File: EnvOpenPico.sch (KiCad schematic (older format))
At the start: 37 parts, among them J2 Conn_01x02, J3 Conn_02x18_Odd_Even, J4 Conn_02x18_Odd_Even, J5 Conn_01x03_Male, U1 SPX3819M5-L-3-3, U2 W25Q128JVPIQ, U3 RP2040, X1 XO 32 12Mhz

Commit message: Corrected some notes
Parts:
- D3: value LED 0402 -> LED 0402 YELLOW
- J2: value Conn_01x02 -> B3U-1000P
- R3, R4: value 27 -> 27 0402 Resistor
- e1: value USB_C -> TYPE-C-31-M-12
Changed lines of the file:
@@
 P 1000 1750
 F 0 "e1" H 750 2150 50  0000 R CNN
-F 1 "USB_C" H 950 950 50  0000 R CNN
+F 1 "TYPE-C-31-M-12" H 1250 950 50  0000 R CNN
 F 2 "Connector_USB:USB_C_Receptacle_HRO_TYPE-C-31-M-12" H 1150 1700 50  0001 C CNN
 F 3 "~" H 1150 1700 50  0001 C CNN
@@
 P 9650 4100
 F 0 "R4" V 9443 4100 50  0000 C CNN
-F 1 "27" V 9534 4100 50  0000 C CNN
+F 1 "27 0402 Resistor" V 9534 4100 50  0000 C CNN
 F 2 "Capacitor_SMD:C_0402_1005Metric" V 9580 4100 50  0001 C CNN
 F 3 "~" H 9650 4100 50  0001 C CNN
@@
 P 1050 4950
 F 0 "J2" H 1100 5100 50  0000 C CNN
-F 1 "Conn_01x02" H 1050 4850 50  0000 C CNN
+F 1 "B3U-1000P" H 1050 4850 50  0000 C CNN
 F 2 "Button_Switch_SMD:SW_SPST_B3U-1000P" H 1050 4950 50  0001 C CNN
 F 3 "~" H 1050 4950 50  0001 C CNN
@@
 P 9650 3800
 F 0 "R3" V 9443 3800 50  0000 C CNN
-F 1 "27" V 9534 3800 50  0000 C CNN
+F 1 "27 0402 Resistor" V 9534 3800 50  0000 C CNN
 F 2 "Capacitor_SMD:C_0402_1005Metric" V 9580 3800 50  0001 C CNN
 F 3 "~" H 9650 3800 50  0001 C CNN
@@
 P 14800 7600
 F 0 "D3" H 14750 7350 50  0000 C CNN
-F 1 "LED 0402" H 14600 7450 50  0000 C CNN
+F 1 "LED 0402 YELLOW" H 14600 7450 50  0000 C CNN
 F 2 "LED_SMD:LED_0402_1005Metric" H 14800 7600 50  0001 C CNN
 F 3 "~" H 14800 7600 50  0001 C CNN

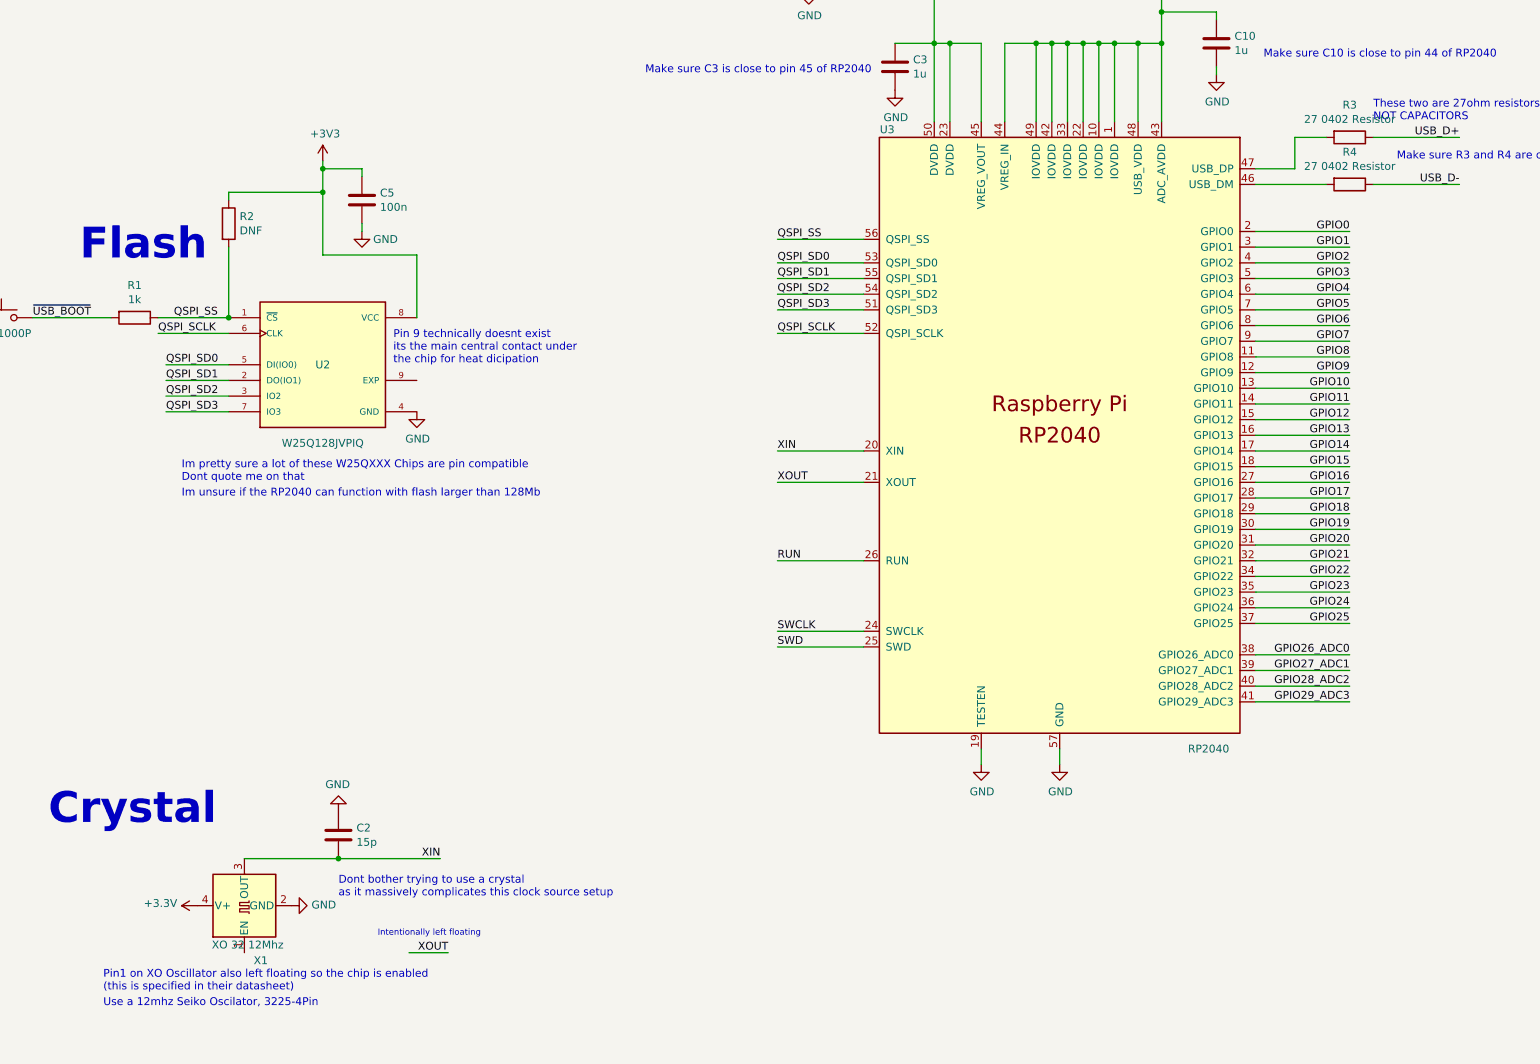
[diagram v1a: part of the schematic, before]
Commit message: Adjusted lables and notes some more for BOM export
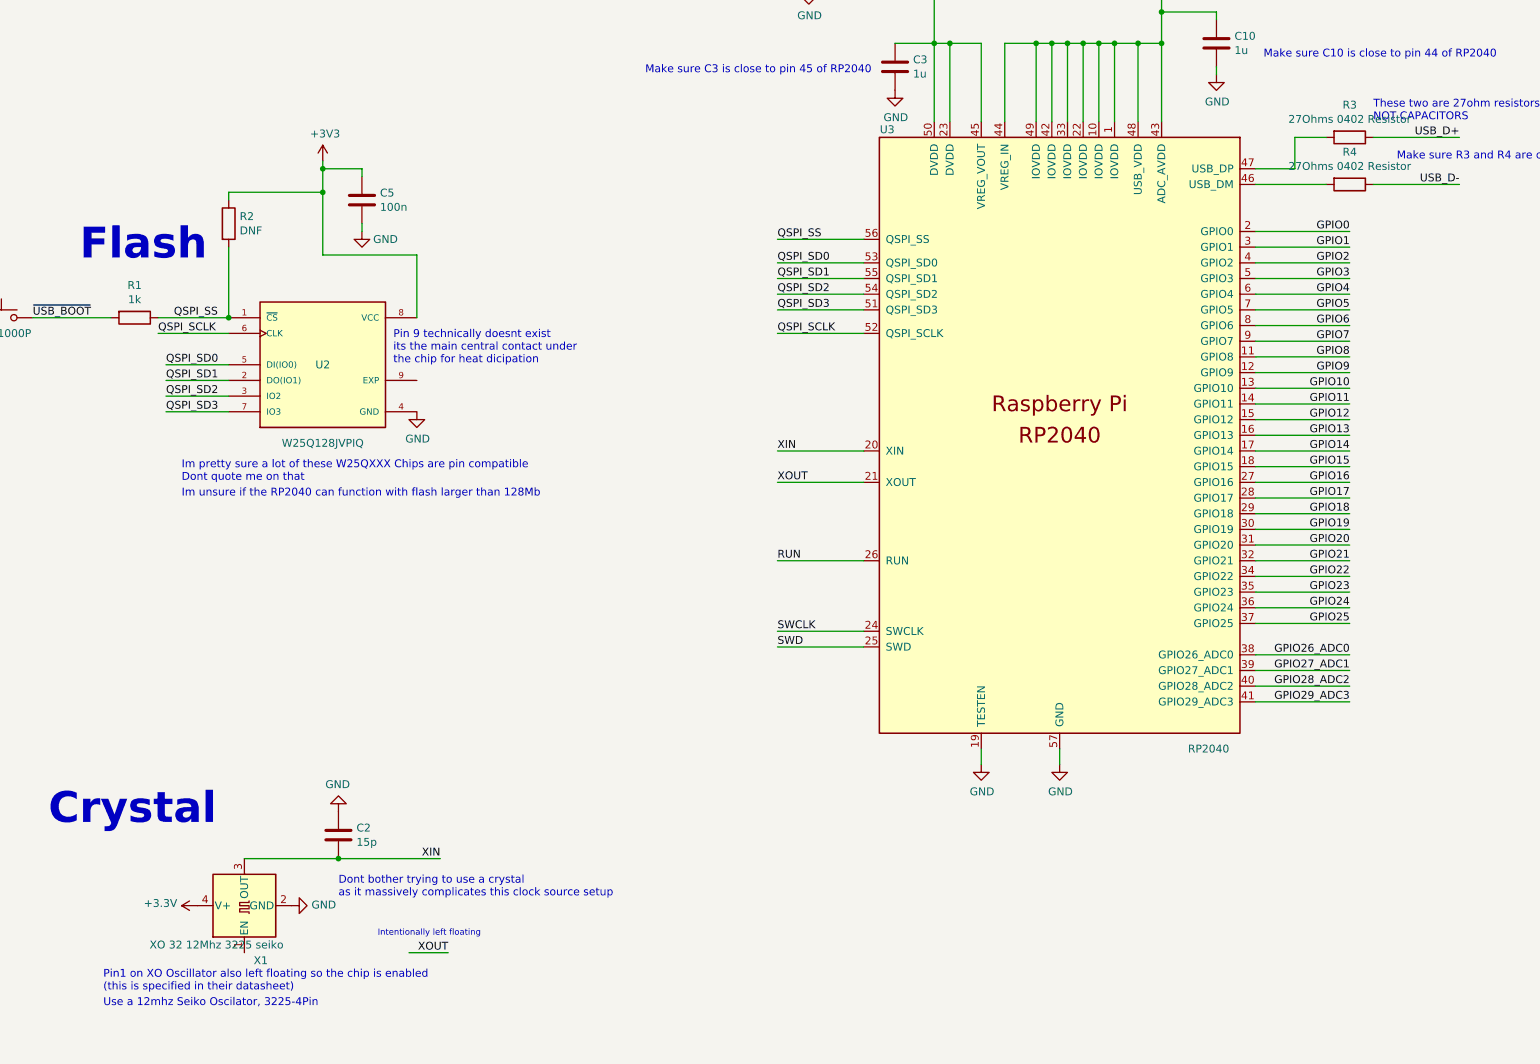
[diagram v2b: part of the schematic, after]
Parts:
- R3, R4: value 27 0402 Resistor -> 27Ohms 0402 Resistor
- U2: MANUFACTURER Winbond Electronics Corp. -> (none)
- X1: value XO 32 12Mhz -> XO 32 12Mhz 3225 seiko
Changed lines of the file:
@@
 P 9650 4100
 F 0 "R4" V 9443 4100 50  0000 C CNN
-F 1 "27 0402 Resistor" V 9534 4100 50  0000 C CNN
+F 1 " 27Ohms 0402 Resistor" V 9534 4100 50  0000 C CNN
 F 2 "Capacitor_SMD:C_0402_1005Metric" V 9580 4100 50  0001 C CNN
 F 3 "~" H 9650 4100 50  0001 C CNN
@@
 P 9650 3800
 F 0 "R3" V 9443 3800 50  0000 C CNN
-F 1 "27 0402 Resistor" V 9534 3800 50  0000 C CNN
+F 1 " 27Ohms  0402 Resistor" V 9534 3800 50  0000 C CNN
 F 2 "Capacitor_SMD:C_0402_1005Metric" V 9580 3800 50  0001 C CNN
 F 3 "~" H 9650 3800 50  0001 C CNN
@@
 P 2600 8700
 F 0 "X1" V 2250 8550 50  0000 L CNN
-F 1 "XO 32 12Mhz" V 2350 8450 50  0000 L CNN
+F 1 "XO 32 12Mhz 3225 seiko" V 2350 8450 50  0000 L CNN
 F 2 "Crystal:Crystal_SMD_SeikoEpson_TSX3225-4Pin_3.2x2.5mm" H 3300 8350 50  0001 C CNN
 F 3 "http://cdn-reichelt.de/documents/datenblatt/B400/XO32.pdf" H 2500 8700 50  0001 C CNN
@@
 F 2 "" H 3100 5250 50  0001 L BNN
 F 3 "" H 3100 5250 50  0001 L BNN
-F 4 "Winbond Electronics Corp." H 3100 5250 50  0001 L BNN "MANUFACTURER"
 	1    3100 5250
 	1    0    0    -1

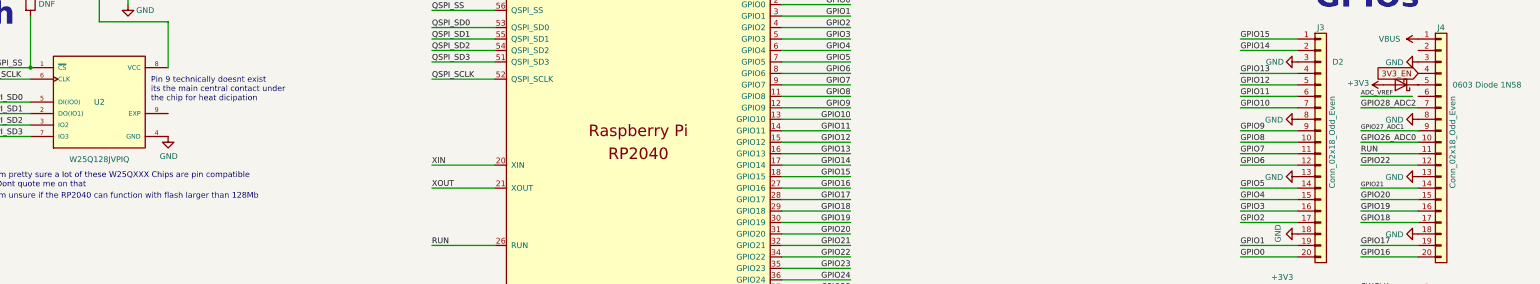
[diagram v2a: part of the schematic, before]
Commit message: some more adjustments to correct auto filling fields in JLCPCB
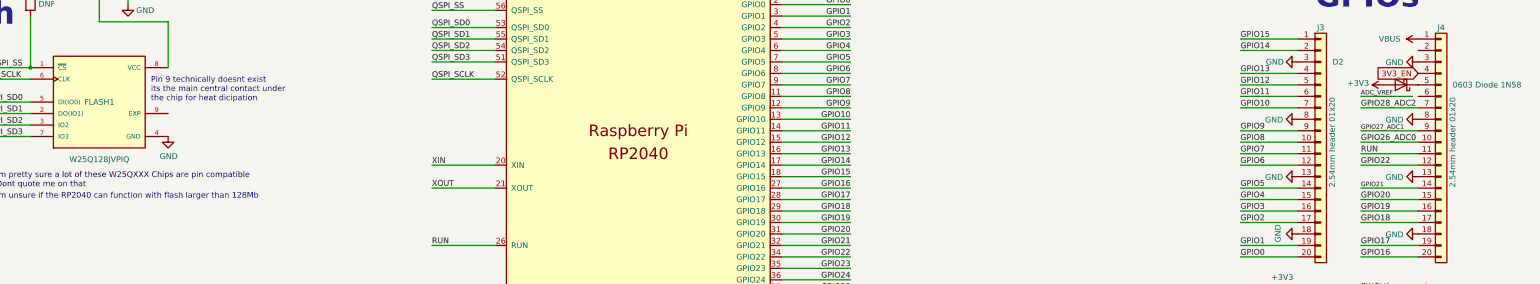
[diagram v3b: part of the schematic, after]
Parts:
- D2: footprint Diode_SMD:D_0603_1608Metri -> Diode_SMD:D_0603_1608Metric
- FLASH1: renamed from U2; footprint (none) -> Package_SON:WSON-8-1EP_6x5mm_P1.27mm_EP3.4x4.3mm
- J3, J4: value Conn_02x18_Odd_Even -> 2.54mm header 01x20
- e1: footprint Connector_USB:USB_C_Receptacle_HRO_TYPE-C-31-M-12 -> HRO-TYPE-C31-M-12:HRO-TYPE-C-31-M-12
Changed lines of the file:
@@
 F 0 "e1" H 750 2150 50  0000 R CNN
 F 1 "TYPE-C-31-M-12" H 1250 950 50  0000 R CNN
-F 2 "Connector_USB:USB_C_Receptacle_HRO_TYPE-C-31-M-12" H 1150 1700 50  0001 C CNN
+F 2 "HRO-TYPE-C31-M-12:HRO-TYPE-C-31-M-12" H 1150 1700 50  0001 C CNN
 F 3 "~" H 1150 1700 50  0001 C CNN
 	1    1000 1750
@@
 P 14800 5600
 F 0 "J4" H 14800 6600 50  0000 C CNN
-F 1 "Conn_02x18_Odd_Even" V 14900 5600 50  0000 C CNN
+F 1 "2.54mm header 01x20" V 14900 5600 50  0000 C CNN
 F 2 "Connector_PinHeader_2.54mm:PinHeader_1x20_P2.54mm_Vertical" H 14800 5600 50  0001 C CNN
 F 3 "~" H 14800 5600 50  0001 C CNN
@@
 P 13750 5600
 F 0 "J3" H 13750 6600 50  0000 C CNN
-F 1 "Conn_02x18_Odd_Even" V 13850 5600 50  0000 C CNN
+F 1 "2.54mm header 01x20" V 13850 5600 50  0000 C CNN
 F 2 "Connector_PinHeader_2.54mm:PinHeader_1x20_P2.54mm_Vertical" H 13750 5600 50  0001 C CNN
 F 3 "~" H 13750 5600 50  0001 C CNN
@@
 F 0 "D2" H 15000 4900 50  0000 C CNN
 F 1 "0603 Diode 1N58" H 13700 5100 50  0000 C CNN
-F 2 "Diode_SMD:D_0603_1608Metri" H 14450 5100 50  0001 C CNN
+F 2 "Diode_SMD:D_0603_1608Metric" H 14450 5100 50  0001 C CNN
 F 3 "~" H 14450 5100 50  0001 C CNN
 	1    14450 5100
@@
 3V3_EN
 $Comp
-L W25Q256JVEIQ_TR:W25Q256JVEIQ_TR U2
+L W25Q256JVEIQ_TR:W25Q256JVEIQ_TR FLASH1
 U 1 1 608EDADA
 P 3100 5250
-F 0 "U2" H 3100 5250 50  0000 C CNN
+F 0 "FLASH1" H 3100 5250 50  0000 C CNN
 F 1 "W25Q128JVPIQ" H 3100 4750 50  0000 C CNN
-F 2 "" H 3100 5250 50  0001 L BNN
+F 2 "Package_SON:WSON-8-1EP_6x5mm_P1.27mm_EP3.4x4.3mm" H 3100 5250 50  0001 L BNN
 F 3 "" H 3100 5250 50  0001 L BNN
 	1    3100 5250

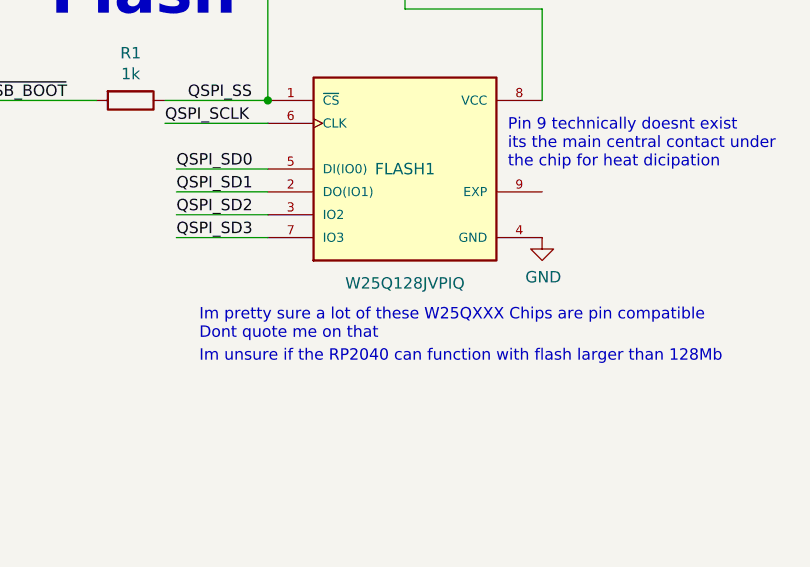
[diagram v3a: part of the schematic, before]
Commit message: Replaced Flash footprint with USON-8/3x2mm to match received samples
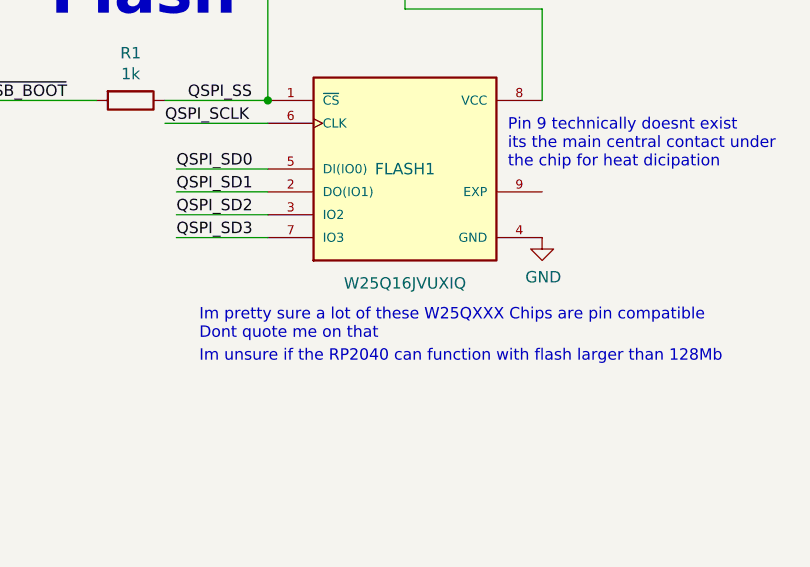
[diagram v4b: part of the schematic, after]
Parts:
- FLASH1: value W25Q128JVPIQ -> W25Q16JVUXIQ; footprint Package_SON:WSON-8-1EP_6x5mm_P1.27mm_EP3.4x4.3mm -> Package_SON:SON-8-1EP_3x2mm_P0.5mm_EP1.4x1.6mm
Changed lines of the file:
@@
 P 3100 5250
 F 0 "FLASH1" H 3100 5250 50  0000 C CNN
-F 1 "W25Q128JVPIQ" H 3100 4750 50  0000 C CNN
-F 2 "Package_SON:WSON-8-1EP_6x5mm_P1.27mm_EP3.4x4.3mm" H 3100 5250 50  0001 L BNN
+F 1 "W25Q16JVUXIQ" H 3100 4750 50  0000 C CNN
+F 2 "Package_SON:SON-8-1EP_3x2mm_P0.5mm_EP1.4x1.6mm" H 3100 5250 50  0001 L BNN
 F 3 "" H 3100 5250 50  0001 L BNN
 	1    3100 5250
